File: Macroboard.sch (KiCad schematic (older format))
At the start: 49 parts, among them Q1 Q_NJFET_DGS, SW1 SW_Push, U1 ATmega32U4-AU, Y1 16MHz

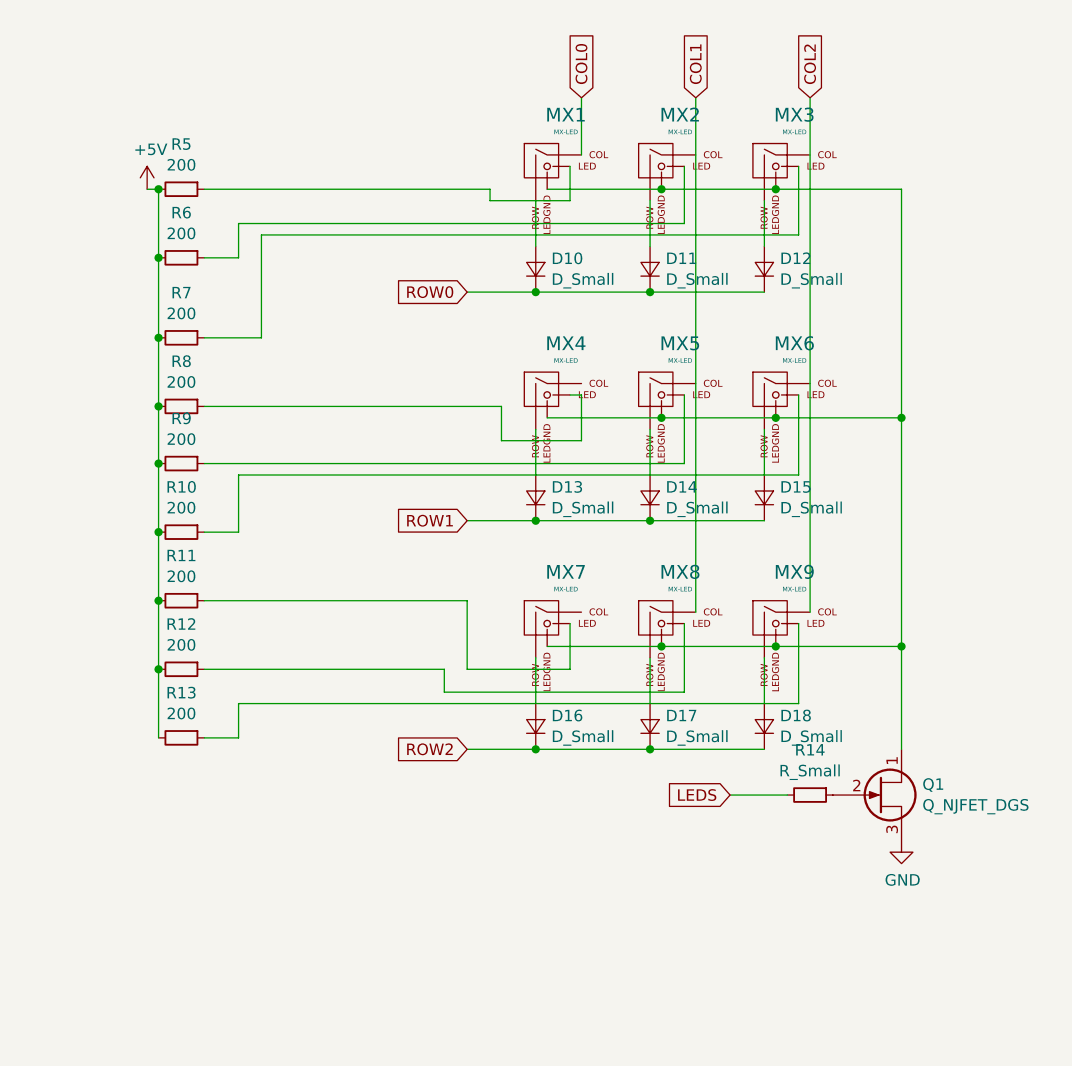
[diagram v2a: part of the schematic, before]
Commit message: added fet
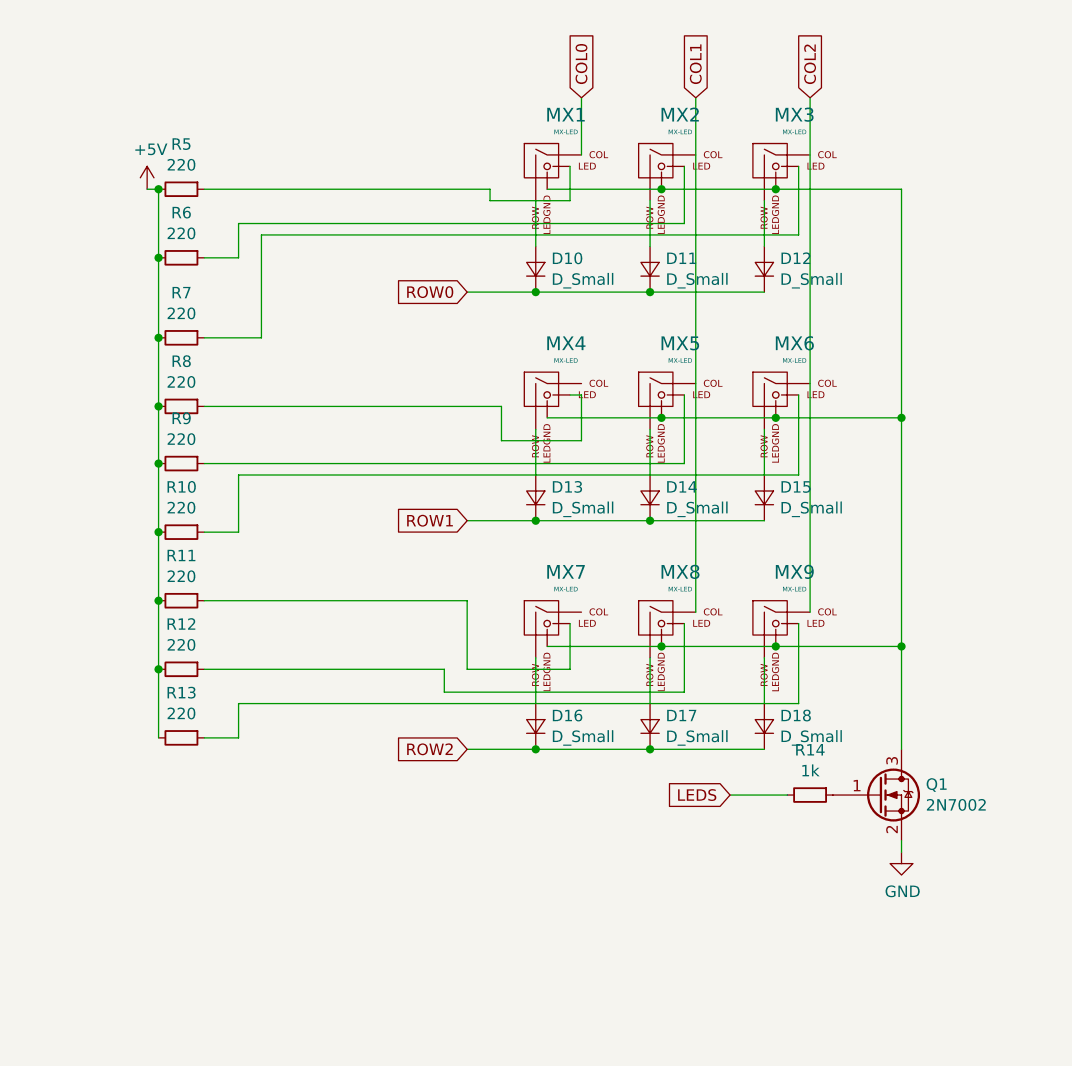
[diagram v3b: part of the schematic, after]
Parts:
- removed Q1: Q_NJFET_DGS, symbol Device:Q_NJFET_DGS
- added Q1: 2N7002, Package_TO_SOT_SMD:SOT-23, symbol Transistor_FET:2N7002
- R10, R11, R12, R13, R5, R6, R7, R8, R9: value 200 -> 220
- R14: value R_Small -> 1k
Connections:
- wire segments 137 -> 138
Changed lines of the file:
@@
-	1    0    0    -1
-$EndComp
-$Comp
-L power:GND #PWR0114
-U 1 1 5DC016F3
-P 10900 4250
-F 0 "#PWR0114" H 10900 4000 50  0001 C CNN
-F 1 "GND" H 10905 4077 50  0000 C CNN
-F 2 "" H 10900 4250 50  0001 C CNN
-F 3 "" H 10900 4250 50  0001 C CNN
-	1    10900 4250
 	1    0    0    -1
 $EndComp
@@
 P 7750 1400
 F 0 "R5" V 7554 1400 50  0000 C CNN
-F 1 "200" V 7645 1400 50  0000 C CNN
+F 1 "220" V 7645 1400 50  0000 C CNN
 F 2 "Resistor_SMD:R_0603_1608Metric_Pad1.05x0.95mm_HandSolder" H 7750 1400 50  0001 C CNN
 F 3 "~" H 7750 1400 50  0001 C CNN
@@
 P 7750 1700
 F 0 "R6" V 7554 1700 50  0000 C CNN
-F 1 "200" V 7645 1700 50  0000 C CNN
+F 1 "220" V 7645 1700 50  0000 C CNN
 F 2 "Resistor_SMD:R_0603_1608Metric_Pad1.05x0.95mm_HandSolder" H 7750 1700 50  0001 C CNN
 F 3 "~" H 7750 1700 50  0001 C CNN
@@
 P 7750 2050
 F 0 "R7" V 7554 2050 50  0000 C CNN
-F 1 "200" V 7645 2050 50  0000 C CNN
+F 1 "220" V 7645 2050 50  0000 C CNN
 F 2 "Resistor_SMD:R_0603_1608Metric_Pad1.05x0.95mm_HandSolder" H 7750 2050 50  0001 C CNN
 F 3 "~" H 7750 2050 50  0001 C CNN
@@
 P 7750 2350
 F 0 "R8" V 7554 2350 50  0000 C CNN
-F 1 "200" V 7645 2350 50  0000 C CNN
+F 1 "220" V 7645 2350 50  0000 C CNN
 F 2 "Resistor_SMD:R_0603_1608Metric_Pad1.05x0.95mm_HandSolder" H 7750 2350 50  0001 C CNN
 F 3 "~" H 7750 2350 50  0001 C CNN
@@
 P 7750 2600
 F 0 "R9" V 7554 2600 50  0000 C CNN
-F 1 "200" V 7645 2600 50  0000 C CNN
+F 1 "220" V 7645 2600 50  0000 C CNN
 F 2 "Resistor_SMD:R_0603_1608Metric_Pad1.05x0.95mm_HandSolder" H 7750 2600 50  0001 C CNN
 F 3 "~" H 7750 2600 50  0001 C CNN
@@
 P 7750 2900
 F 0 "R10" V 7554 2900 50  0000 C CNN
-F 1 "200" V 7645 2900 50  0000 C CNN
+F 1 "220" V 7645 2900 50  0000 C CNN
 F 2 "Resistor_SMD:R_0603_1608Metric_Pad1.05x0.95mm_HandSolder" H 7750 2900 50  0001 C CNN
 F 3 "~" H 7750 2900 50  0001 C CNN
@@
 P 7750 3200
 F 0 "R11" V 7554 3200 50  0000 C CNN
-F 1 "200" V 7645 3200 50  0000 C CNN
+F 1 "220" V 7645 3200 50  0000 C CNN
 F 2 "Resistor_SMD:R_0603_1608Metric_Pad1.05x0.95mm_HandSolder" H 7750 3200 50  0001 C CNN
 F 3 "~" H 7750 3200 50  0001 C CNN
@@
 P 7750 3500
 F 0 "R12" V 7554 3500 50  0000 C CNN
-F 1 "200" V 7645 3500 50  0000 C CNN
+F 1 "220" V 7645 3500 50  0000 C CNN
 F 2 "Resistor_SMD:R_0603_1608Metric_Pad1.05x0.95mm_HandSolder" H 7750 3500 50  0001 C CNN
 F 3 "~" H 7750 3500 50  0001 C CNN
@@
 P 7750 3800
 F 0 "R13" V 7554 3800 50  0000 C CNN
-F 1 "200" V 7645 3800 50  0000 C CNN
+F 1 "220" V 7645 3800 50  0000 C CNN
 F 2 "Resistor_SMD:R_0603_1608Metric_Pad1.05x0.95mm_HandSolder" H 7750 3800 50  0001 C CNN
 F 3 "~" H 7750 3800 50  0001 C CNN
@@
 Wire Wire Line
 	9450 1450 9450 1300
-$Comp
-L Device:Q_NJFET_DGS Q1
-U 1 1 5DCAA613
-P 10800 4050
-F 0 "Q1" H 10991 4096 50  0000 L CNN
-F 1 "Q_NJFET_DGS" H 10991 4005 50  0000 L CNN
-F 2 "" H 11000 4150 50  0001 C CNN
-F 3 "~" H 10800 4050 50  0001 C CNN
-	1    10800 4050
-	1    0    0    -1
-$EndComp
 $Comp
 L power:+5V #PWR0115
@@
 P 10500 4050
 F 0 "R14" V 10304 4050 50  0000 C CNN
-F 1 "R_Small" V 10395 4050 50  0000 C CNN
+F 1 "1k" V 10395 4050 50  0000 C CNN
 F 2 "Resistor_SMD:R_0603_1608Metric_Pad1.05x0.95mm_HandSolder" H 10500 4050 50  0001 C CNN
 F 3 "~" H 10500 4050 50  0001 C CNN
@@
 Wire Wire Line
 	8000 2650 10450 2650
+$Comp
+L Transistor_FET:2N7002 Q1
+U 1 1 5DB5AEA1
+P 10800 4050
+F 0 "Q1" H 11006 4096 50  0000 L CNN
+F 1 "2N7002" H 11006 4005 50  0000 L CNN
+F 2 "Package_TO_SOT_SMD:SOT-23" H 11000 3975 50  0001 L CIN
+F 3 "https://www.fairchildsemi.com/datasheets/2N/2N7002.pdf" H 10800 4050 50  0001 L CNN
+	1    10800 4050
+	1    0    0    -1
+$EndComp
+$Comp
+L power:GND #PWR0114
+U 1 1 5DB5E4D1
+P 10900 4300
+F 0 "#PWR0114" H 10900 4050 50  0001 C CNN
+F 1 "GND" H 10905 4127 50  0000 C CNN
+F 2 "" H 10900 4300 50  0001 C CNN
+F 3 "" H 10900 4300 50  0001 C CNN
+	1    10900 4300
+	1    0    0    -1
+$EndComp
+Wire Wire Line
+	10900 4250 10900 4300
 $EndSCHEMATC

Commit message: new button and hotfixin
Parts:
- SW1: footprint random-keyboard-parts:SKQG-1155865 -> Button_Switch_THT:SW_PUSH_6mm_H4.3mm
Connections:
- net labels added: LED_TRN, L_MX1, L_MX2, L_MX3, L_MX4, L_MX5, L_MX6, L_MX7, L_MX8, L_MX9
- wire segments 138 -> 123
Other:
- moved on the sheet: D16, D17, D18, Q1, R10, R11, R12, R13, R14, R5, R6, R7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
